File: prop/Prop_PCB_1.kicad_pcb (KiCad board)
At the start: 4 copper layers, 63.5 x 63.5 mm, 16 parts, among them J1 1984989, J2 1984989, J3 1984989, J4 1984989, J5 CAS_stacking, J6 Conn_01x02, J7 1984989, U1 L298P, U1301 MAX6675ISA+, U2 SN74LVC8T245DBR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

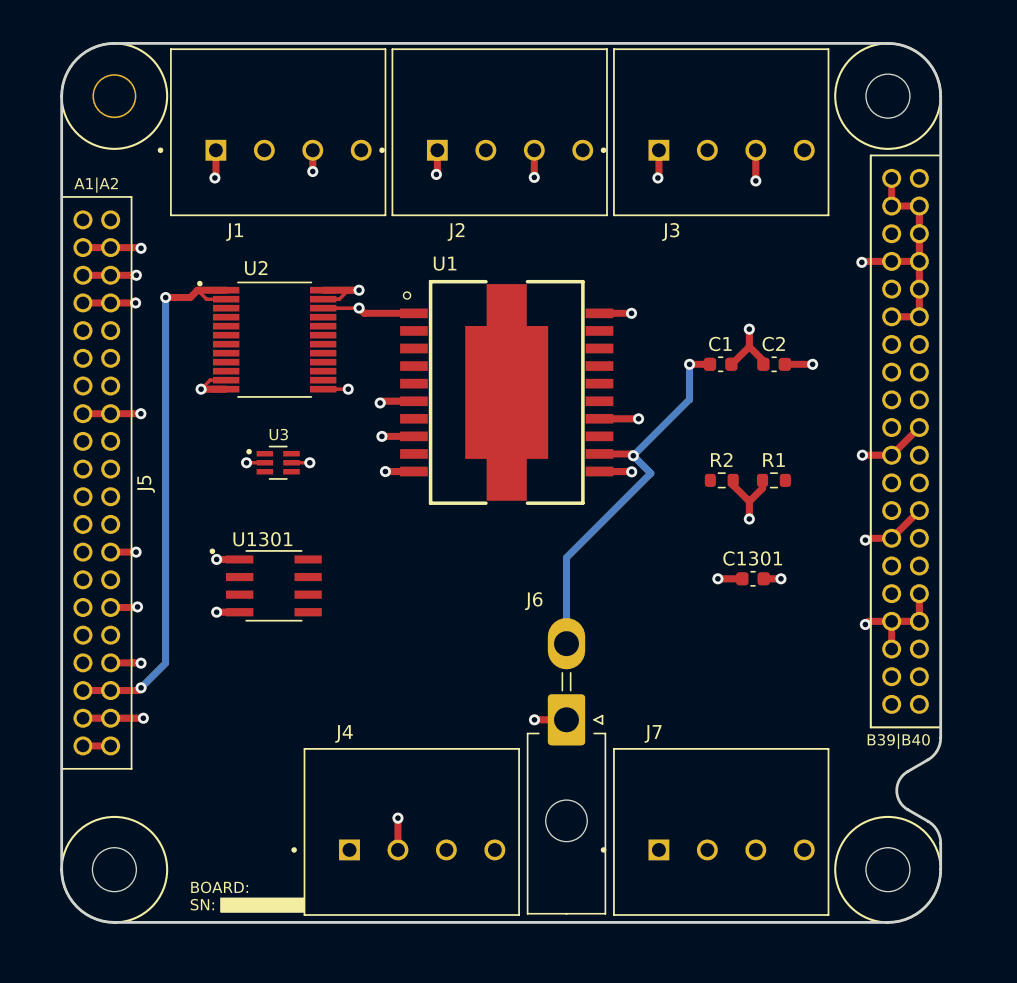
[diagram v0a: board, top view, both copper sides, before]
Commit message: Almost finished wiring PCB.
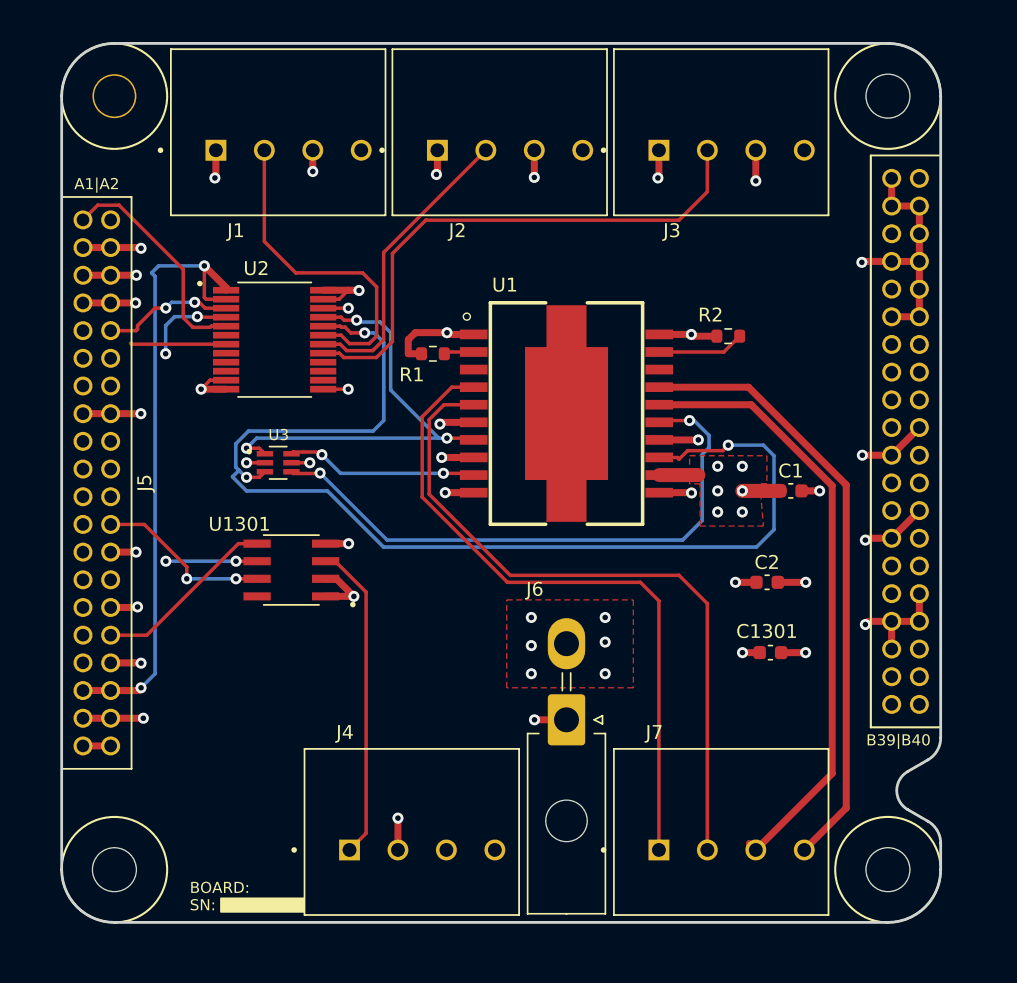
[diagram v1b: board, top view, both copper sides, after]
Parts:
- moved R1 26.3 mm to (80.8, 67.1)
- moved C2 15.8 mm to (104.9, 83.6)
- moved C1 10.5 mm to (106.6, 77.0)
- moved R2 10.4 mm to (102.1, 65.8), turned to 180 degrees
- moved C1301 5.48 mm to (105.2, 88.6), turned to 180 degrees
- moved U1 4.58 mm to (90.4, 71.4)
- moved U1301 1.70 mm to (70.5, 82.7), turned to 180 degrees
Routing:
- net Sol2: track 0.00 -> 83.2 mm, vias 0 -> 3
- net Sol1Lead2: track 0.00 -> 50.2 mm
- net Sol1Lead1: track 0.00 -> 48.6 mm
- net Sol2Lead1: track 0.00 -> 44.2 mm
- net Sol2Lead2: track 0.00 -> 44.1 mm
- net Sol2': track 0.00 -> 42.8 mm, vias 0 -> 2
- net PWM3: track 0.00 -> 39.6 mm
- net Sol1: track 0.00 -> 32.7 mm, vias 0 -> 3
- net PWM1: track 0.00 -> 24.0 mm
- net +24V: track 28.9 -> 5.55 mm, vias 2 -> 12
- net /MAX6675ISA/T+: track 0.00 -> 23.0 mm
- net PWM2: track 0.00 -> 21.6 mm
- net PWM1_33: track 0.00 -> 16.5 mm
- net Sol1': track 0.00 -> 13.9 mm, vias 0 -> 2
- net SPI0_SCK: track 0.00 -> 13.3 mm
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- added copper zone on F.Cu, net +24V
- added copper zone on In2.Cu, net +24V

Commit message: Passed DRC (kind of).
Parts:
- moved J4 0.25 mm to (79.0, 101.6)
- moved J6 0.17 mm to (90.2, 93.5)
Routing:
- net PWM2_33: track 0.00 -> 15.1 mm
- net Sol2_33: track 6.74 -> 13.7 mm
- net CS4: track 7.53 -> 14.1 mm
- net PWM3_33: track 6.94 -> 10.8 mm
- net +24V: track 5.55 -> 8.39 mm
- net PWM1_33: track 16.5 -> 17.8 mm
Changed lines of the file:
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@@
   )
   (footprint "star-common-lib:PHOENIX_1984989" (layer "F.Cu")
-    (at 79.248 101.6)
+    (at 79 101.6)
     (property "MANUFACTURER" "Phoenix Contact")
     (property "MAXIMUM_PACKAGE_HEIGHT" "13.1mm")
@@
   )
   (footprint "Connector_Molex:Molex_Mini-Fit_Jr_5569-02A2_2x01_P4.20mm_Horizontal" (layer "F.Cu")
-    (at 90.424 93.499 180)
+    (at 90.25 93.499 180)
     (descr "Molex Mini-Fit Jr. Power Connectors, old mpn/engineering number: 5569-02A2, example for new mpn: 39-30-0020, 1 Pins per row, Mounting: Snap-in Plastic Peg PCB Lock (http://www.molex.com/pdm_docs/sd/039300020_sd.pdf), generated with kicad-footprint-generator")
     (tags "connector Molex Mini-Fit_Jr top entryplastic_peg")
@@
   (segment (start 113.915 74.385) (end 115.915 72.385) (width 0.508) (layer "F.Cu") (net 1))
   (segment (start 65.837 69.615) (end 64.027 69.615) (width 0.508) (layer "F.Cu") (net 1))
-  (segment (start 78.248 102.9) (end 78.248 100.6) (width 0.508) (layer "F.Cu") (net 1))
+  (segment (start 78 102.9) (end 78 100.6) (width 0.508) (layer "F.Cu") (net 1))
   (segment (start 57.495 59.385) (end 59.639 59.385) (width 0.508) (layer "F.Cu") (net 1))
   (segment (start 107.403 76.96) (end 107.431 76.96) (width 0.508) (layer "F.Cu") (net 1))
@@
   (via (at 59.8569 93.3849) (size 0.8) (drill 0.4) (layers "F.Cu" "B.Cu") (net 1))
   (via (at 59.436 85.344) (size 0.8) (drill 0.4) (layers "F.Cu" "B.Cu") (net 1))
-  (via (at 78.248 100.6) (size 0.8) (drill 0.4) (layers "F.Cu" "B.Cu") (net 1))
+  (via (at 78 100.6) (size 0.8) (drill 0.4) (layers "F.Cu" "B.Cu") (net 1))
   (via (at 88.098 54.316) (size 0.8) (drill 0.4) (layers "F.Cu" "B.Cu") (net 1))
   (via (at 112.014 80.518) (size 0.8) (drill 0.4) (layers "F.Cu" "B.Cu") (net 1))
@@
   (segment (start 60.106847 87.385) (end 57.495 87.385) (width 0.254) (layer "F.Cu") (net 4))
   (segment (start 68.072 82.042) (end 68.762 82.042) (width 0.254) (layer "F.Cu") (net 5))
+  (segment (start 61.152589 82.371911) (end 56.481911 82.371911) (width 0.2032) (layer "F.Cu") (net 5))
+  (segment (start 61.4825 82.042) (end 61.152589 82.371911) (width 0.2032) (layer "F.Cu") (net 5))
   (segment (start 68.072 82.042) (end 66.548 82.042) (width 0.254) (layer "F.Cu") (net 5))
   (segment (start 66.294 82.042) (end 66.548 82.042) (width 0.254) (layer "F.Cu") (net 5))
+  (segment (start 56.481911 82.371911) (end 55.495 81.385) (width 0.2032) (layer "F.Cu") (net 5))
   (via (at 66.548 82.042) (size 0.8) (drill 0.4) (layers "F.Cu" "B.Cu") (net 5))
   (via (at 61.4825 82.042) (size 0.8) (drill 0.4) (layers "F.Cu" "B.Cu") (net 5))
@@
   (segment (start 72.755238 74.347841) (end 74.099397 75.692) (width 0.254) (layer "B.Cu") (net 13))
   (segment (start 97.124 75.819) (end 99.949 75.819) (width 1.016) (layer "F.Cu") (net 14))
+  (segment (start 93.103 87.999) (end 93.218 87.884) (width 1.016) (layer "F.Cu") (net 14))
   (segment (start 105.853 76.96) (end 103.126 76.96) (width 1.016) (layer "F.Cu") (net 14))
+  (segment (start 90.424 87.999) (end 93.103 87.999) (width 1.016) (layer "F.Cu") (net 14))
   (via (at 93.218 90.17) (size 0.8) (drill 0.4) (layers "F.Cu" "B.Cu") (net 14))
   (via (at 87.884 90.17) (size 0.8) (drill 0.4) (layers "F.Cu" "B.Cu") (net 14))
@@
   (segment (start 61.897239 63.339261) (end 61.4825 63.754) (width 0.254) (layer "B.Cu") (net 22))
   (segment (start 65.837 64.415) (end 65.803511 64.381511) (width 0.254) (layer "F.Cu") (net 23))
+  (segment (start 61.468 67.056) (end 60.152089 68.371911) (width 0.2032) (layer "F.Cu") (net 23))
   (segment (start 63.798841 64.415) (end 63.755605 64.371764) (width 0.254) (layer "F.Cu") (net 23))
   (segment (start 65.837 64.415) (end 63.798841 64.415) (width 0.254) (layer "F.Cu") (net 23))
+  (segment (start 56.481911 68.371911) (end 55.495 67.385) (width 0.2032) (layer "F.Cu") (net 23))
+  (segment (start 60.152089 68.371911) (end 56.481911 68.371911) (width 0.2032) (layer "F.Cu") (net 23))
   (via (at 63.755605 64.371764) (size 0.8) (drill 0.4) (layers "F.Cu" "B.Cu") (net 23))
   (via (at 61.468 67.056) (size 0.8) (drill 0.4) (layers "F.Cu" "B.Cu") (net 23))
@@
   (segment (start 61.468 65.024) (end 61.468 67.056) (width 0.254) (layer "B.Cu") (net 23))
   (segment (start 65.837 65.065) (end 64.763557 65.065) (width 0.254) (layer "F.Cu") (net 24))
-  (segment (start 58.100689 56.322689) (end 56.557311 56.322689) (width 0.254) (layer "F.Cu") (net 24))
   (segment (start 64.763557 65.065) (end 64.680282 65.148275) (width 0.254) (layer "F.Cu") (net 24))
-  (segment (start 62.738 64.452312) (end 62.738 60.96) (width 0.254) (layer "F.Cu") (net 24))
-  (segment (start 62.738 60.96) (end 58.100689 56.322689) (width 0.254) (layer "F.Cu") (net 24))
+  (segment (start 62.738 58.762) (end 60.348689 56.372689) (width 0.254) (layer "F.Cu") (net 24))
+  (segment (start 60.348689 56.372689) (end 56.507311 56.372689) (width 0.254) (layer "F.Cu") (net 24))
+  (segment (start 56.507311 56.372689) (end 55.495 57.385) (width 0.254) (layer "F.Cu") (net 24))
   (segment (start 64.680282 65.148275) (end 63.433963 65.148275) (width 0.254) (layer "F.Cu") (net 24))
   (segment (start 63.433963 65.148275) (end 62.738 64.452312) (width 0.254) (layer "F.Cu") (net 24))
-  (segment (start 56.557311 56.322689) (end 55.495 57.385) (width 0.254) (layer "F.Cu") (net 24))
-  (segment (start 58.999 66.365) (end 58.928 66.294) (width 0.254) (layer "F.Cu") (net 26))
-  (segment (start 65.837 66.365) (end 58.999 66.365) (width 0.254) (layer "F.Cu") (net 26))
+  (segment (start 62.738 64.452312) (end 62.738 58.762) (width 0.254) (layer "F.Cu") (net 24))
+  (segment (start 60.635 57.385) (end 57.495 57.385) (width 0.254) (layer "F.Cu") (net 25))
+  (segment (start 65.837 65.715) (end 63.359314 65.715) (width 0.254) (layer "F.Cu") (net 25))
+  (segment (start 62.209011 64.564697) (end 62.209011 58.959011) (width 0.254) (layer "F.Cu") (net 25))
+  (segment (start 62.209011 58.959011) (end 60.635 57.385) (width 0.254) (layer "F.Cu") (net 25))
+  (segment (start 63.359314 65.715) (end 62.209011 64.564697) (width 0.254) (layer "F.Cu") (net 25))
+  (segment (start 65.801489 66.329489) (end 58.329489 66.329489) (width 0.254) (layer "F.Cu") (net 26))
+  (segment (start 58.329489 66.329489) (end 58.287067 66.371911) (width 0.2032) (layer "F.Cu") (net 26))
+  (segment (start 56.481911 66.371911) (end 55.495 65.385) (width 0.2032) (layer "F.Cu") (net 26))
+  (segment (start 65.837 66.365) (end 65.801489 66.329489) (width 0.254) (layer "F.Cu") (net 26))
+  (segment (start 58.287067 66.371911) (end 56.481911 66.371911) (width 0.2032) (layer "F.Cu") (net 26))
   (segment (start 77.849042 66.168958) (end 77.849042 59.815042) (width 0.254) (layer "F.Cu") (net 33))
   (segment (start 74.015854 67.015) (end 74.330903 67.330049) (width 0.254) (layer "F.Cu") (net 33))
@@
     (polygon
       (pts
-        (xy 95.25 91.186)
-        (xy 86.106 91.186)
-        (xy 86.106 84.836)
-        (xy 95.25 84.836)
+        (xy 95 91.186)
+        (xy 85.856 91.186)
+        (xy 85.856 84.836)
+        (xy 95 84.836)
       )
     )
@@
         (xy 48.514 41.148)
         (xy 123.19 41.148)
+      )
+    )
+  )
+  (zone (net 14) (net_name "+24V") (layer "In2.Cu") (hatch edge 0.508)
+    (connect_pads (clearance 0.508))
+    (min_thickness 0.254) (filled_areas_thickness no)
+    (fill yes (thermal_gap 0.508) (thermal_bridge_width 0.508))
+    (polygon
+      (pts
+        (xy 105 108.75)
+        (xy 85.5 108.75)
+        (xy 85.5 74.5)
+        (xy 105 74.5)
       )
     )
@@
       )
     )
-  )
-  (zone (net 14) (net_name "+24V") (layer "In2.Cu") (hatch edge 0.508)
-    (connect_pads (clearance 0.508))
-    (min_thickness 0.254) (filled_areas_thickness no)
-    (fill yes (thermal_gap 0.508) (thermal_bridge_width 0.508))
-    (polygon
-      (pts
-        (xy 105.41 74.168)
-        (xy 104.648 109.22)
-        (xy 84.836 108.966)
-        (xy 84.836 73.914)
-      )
-    )
